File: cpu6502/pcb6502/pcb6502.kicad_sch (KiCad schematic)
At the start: 11 parts, among them J1 Power Plug, SW1 Reset, U1 6502, U2 EEPROM, U3 RAM, U4 65C22, U5 74HC00, U6 LCD (HD44780), X1 1MHz

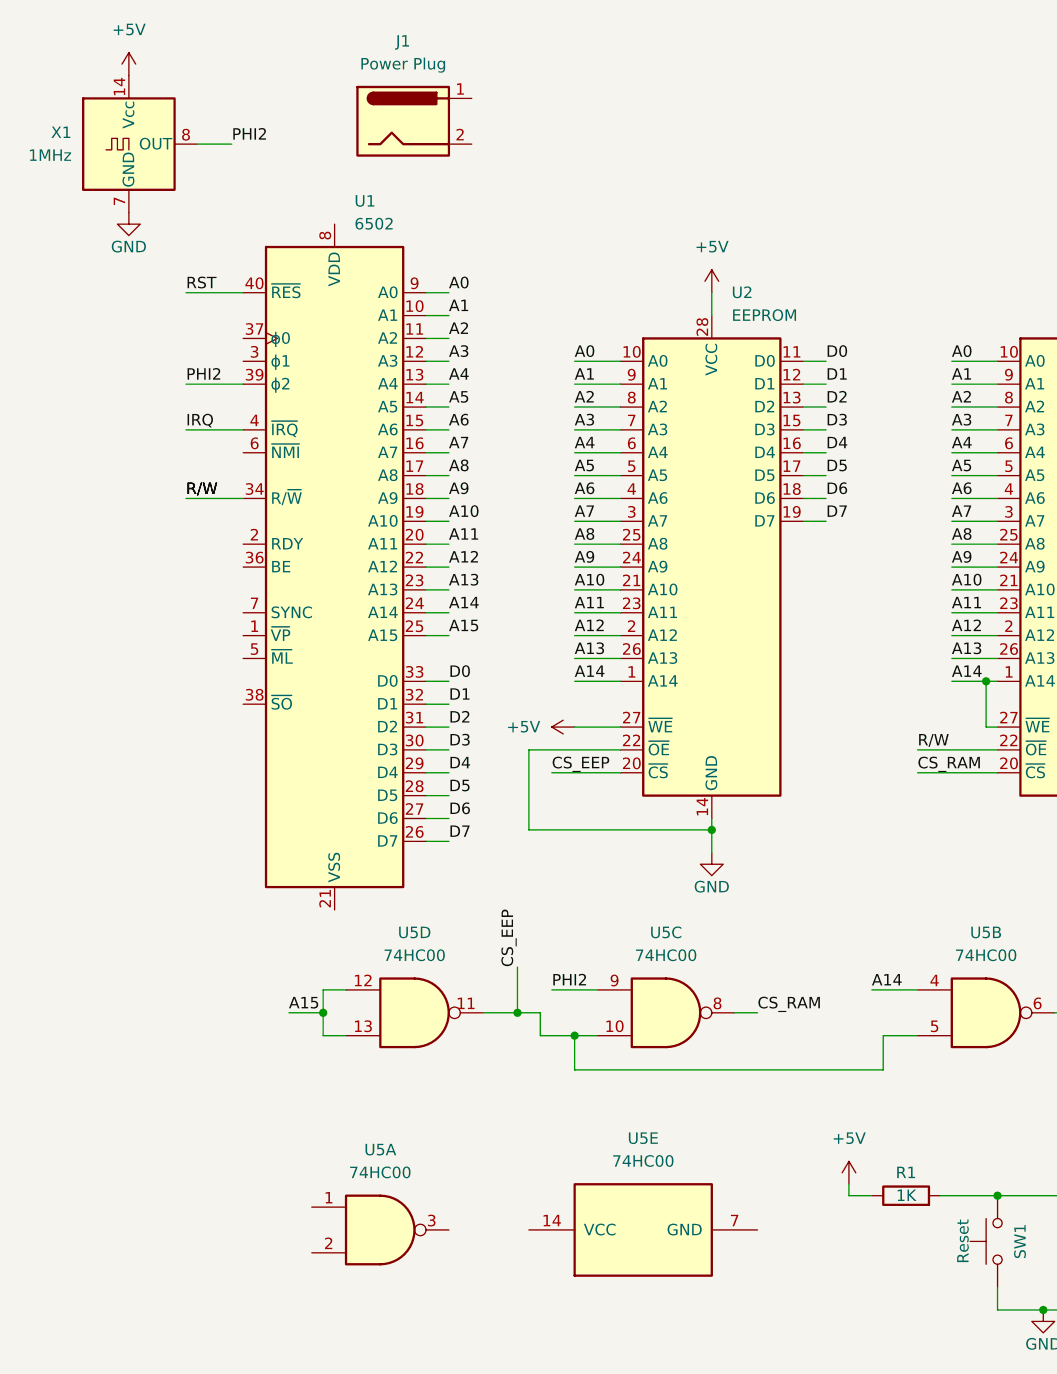
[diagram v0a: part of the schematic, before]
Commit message: connect more pins 6502 PCB
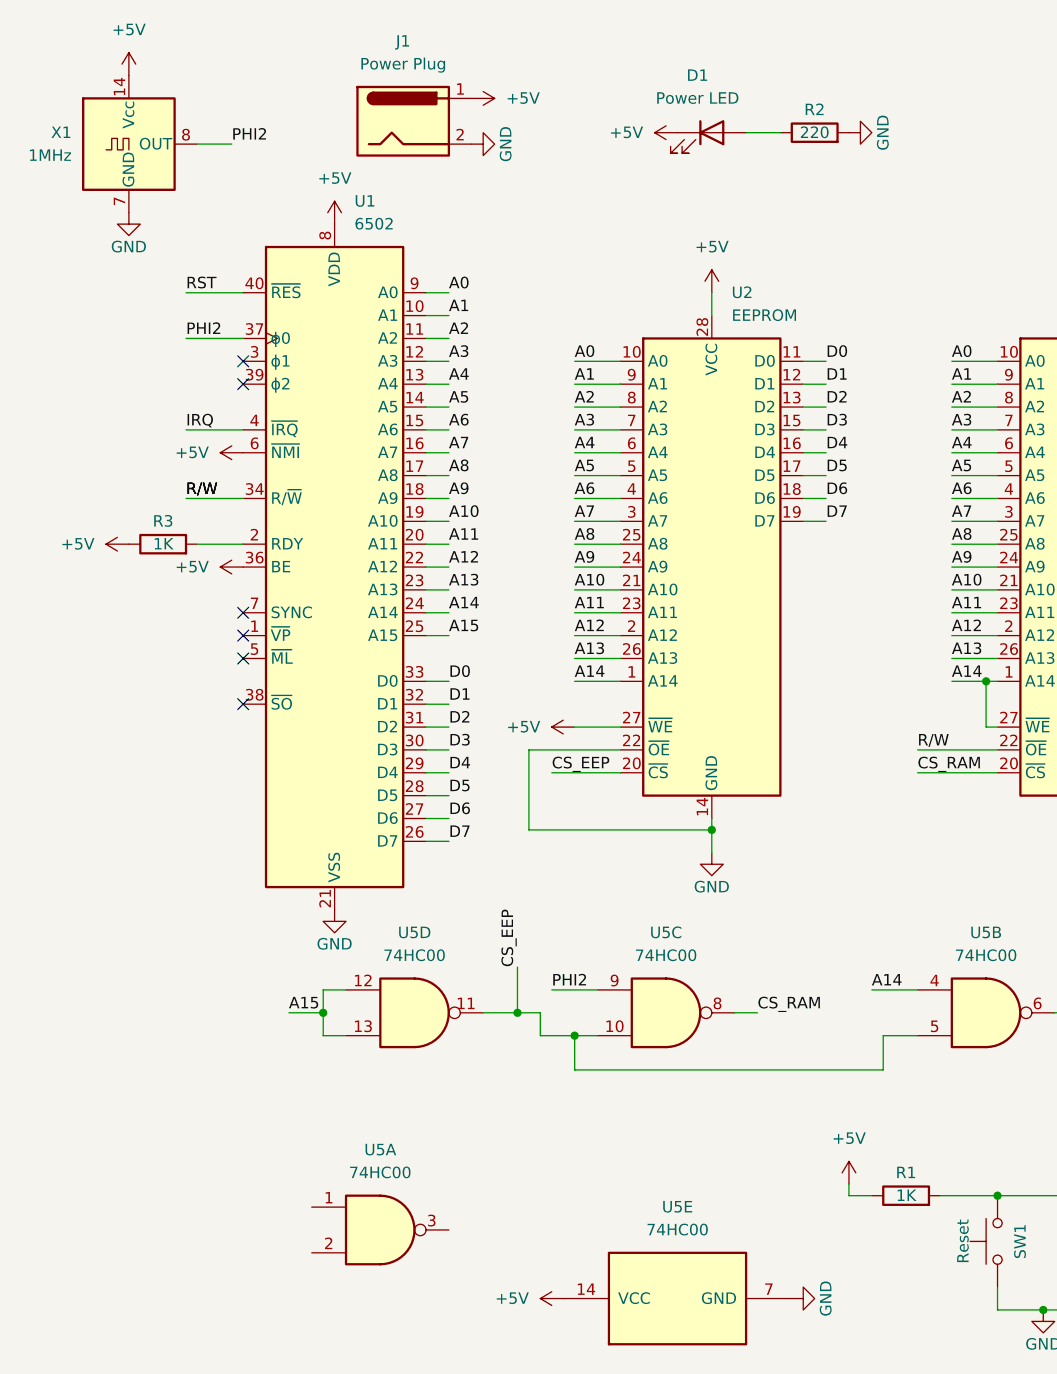
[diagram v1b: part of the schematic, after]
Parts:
- added D1: Power LED, LED_THT:LED_D5.0mm, symbol Device:LED
- added R2: 220, Resistor_THT:R_Axial_DIN0204_L3.6mm_D1.6mm_P7.62mm_Horizontal, symbol Device:R
- added R3: 1K, Resistor_THT:R_Axial_DIN0204_L3.6mm_D1.6mm_P7.62mm_Horizontal, symbol Device:R
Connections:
- net +5V: now also J1.1, U1.36 (BE), U1.6 (~{NMI}), U1.8 (VDD), U5.14 (VCC), D1.1 (K), R3.1
- net GND: now also J1.2, U1.21 (VSS), U5.7 (GND), R2.2
- net PHI2: now also U1.37 (ϕ0); no longer U1.39 (ϕ2)
- net at U1.2 (RDY): now also R3.2
- new net: D1.2 (A), R2.1
- no-connect marks 4 -> 10
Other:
- moved on the sheet: U5E

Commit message: start to add rs232
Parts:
- removed J1: Power Plug, Connector_BarrelJack:BarrelJack_Horizontal, symbol Connector:Barrel_Jack
- added C2, C3, C4, C5: 1uf, Capacitor_THT:C_Disc_D3.0mm_W1.6mm_P2.50mm, symbol Device:C
- added D2: SB140, Diode_THT:D_DO-41_SOD81_P10.16mm_Horizontal, symbol Diode:SB140
- added J1: 5v Power, Connector_BarrelJack:BarrelJack_Horizontal, symbol Connector:Barrel_Jack_MountingPin
- added J2: DE9_Receptacle, Connector_Dsub:DSUB-9_Female_Horizontal_P2.77x2.54mm_EdgePinOffset9.40mm, symbol Connector:DE9_Receptacle
- added RV1: 10K, Potentiometer_THT:Potentiometer_ACP_CA9-V10_Vertical, symbol Device:R_Potentiometer
- added U7: W65C51NxP, Package_DIP:DIP-28_W15.24mm, symbol PCM_65xx-library:W65C51NxP
- added U8: MAX232, Package_DIP:DIP-16_W7.62mm_Socket, symbol Interface_UART:MAX232
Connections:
- net +5V: now also U6.2 (LEDA), U6.4 (VDD), J1.1, U7.15 (VCC)
- net A0: now also U7.13 (RS0)
- net A1: now also U7.14 (RS1)
- net A12: now also U7.2 (CS1)
- net CS2: now also U7.3 (~{CS2})
- net D0: now also U7.18 (D0)
- net D1: now also U7.19 (D1)
- net D2: now also U7.20 (D2)
- net D3: now also U7.21 (D3)
- net D4: now also U7.22 (D4)
- net D5: now also U7.23 (D5)
- net D6: now also U7.24 (D6)
- net D7: now also U7.25 (D7)
- net GND: now also U6.3 (VSS), J1.2, J1.MP (MountPin), RV1.1, U7.1 (VSS)
- net IRQ: now also D2.2 (A)
- net PHI2: now also U7.27 (ϕ2)
- net RST: now also U7.4 (~{RES})
- net R/W: now also U7.28 (R/~{W})
- net LCD_K: now reaches U6.1 (LEDK)
- net LCD_VO: now reaches U6.5 (Vo)
- net LCD_VO: now also RV1.2
- new net: D2.1 (K), U7.26 (~{IRQ})
- no-connect marks 10 -> 11
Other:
- title: (none) -> Chris G 6502

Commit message: finish rs232, re-layour PCB
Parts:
- removed J1: 5v Power, Connector_BarrelJack:BarrelJack_Horizontal, symbol Connector:Barrel_Jack_MountingPin
- added C6: 20pf, Capacitor_THT:C_Disc_D3.0mm_W1.6mm_P2.50mm, symbol Device:C
- added J1: 5v Power, Connector_BarrelJack:BarrelJack_CUI_PJ-102AH_Horizontal, symbol Connector:Barrel_Jack_Switch_MountingPin
- added R4: 1M, Resistor_THT:R_Axial_DIN0204_L3.6mm_D1.6mm_P7.62mm_Horizontal, symbol Device:R
- added Y1: Crystal, Crystal:Crystal_HC49-4H_Vertical, symbol Device:Crystal
- J2: value DE9_Receptacle -> RS232
- U5: footprint Package_DIP:DIP-14_W7.62mm -> Package_DIP:DIP-14_W7.62mm_Socket
- U6: footprint Display:HY1602E -> Display:WC1602A
- U7: footprint Package_DIP:DIP-28_W15.24mm -> Package_DIP:DIP-28_W15.24mm_Socket
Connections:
- net +5V: now also U8.16 (VCC), J1.1
- net GND: now also C4.1, C5.2, J2.5, U8.15 (GND), C6.2, J1.2, J1.3
- net TxD: now reaches U7.10 (TxD)
- net TxD: now also U8.11 (T1IN)
- net RxD: now reaches U7.12 (RxD)
- net RxD: now also U8.12 (R1OUT)
- net XTLA1: now reaches U7.6 (XTAL1)
- net XTLA1: now also R4.2, Y1.2
- net XTAL2: now reaches U7.7 (XTAL2)
- net XTAL2: now also C6.1, R4.1, Y1.1
- net 232_VS+: now reaches C4.2
- net 232_VS+: now also U8.2 (VS+)
- net at C3.1: now also U8.4 (C2+)
- net at C3.2: now also U8.5 (C2-)
- net at U8.1 (C1+): now also C2.1
- net at U8.13 (R1IN): now also J2.3
- net at U8.14 (T1OUT): now also J2.2
- net at U8.3 (C1-): now also C2.2
- net 232_VS-: now reaches U8.6 (VS-)
- net 232_VS-: now also C5.1
- no-connect marks 11 -> 27
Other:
- moved on the sheet: C2, C3, C4, C5, J2

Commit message: routed PCB!
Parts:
- removed C1: 0.1uf, Capacitor_THT:C_Disc_D3.0mm_W1.6mm_P2.50mm, symbol Device:C
- removed J1: 5v Power, Connector_BarrelJack:BarrelJack_CUI_PJ-102AH_Horizontal, symbol Connector:Barrel_Jack_Switch_MountingPin
- removed R1: 1K, Resistor_THT:R_Axial_DIN0204_L3.6mm_D1.6mm_P7.62mm_Horizontal, symbol Device:R
- removed RV1: 10K, Potentiometer_THT:Potentiometer_ACP_CA9-V10_Vertical, symbol Device:R_Potentiometer
- removed U6: LCD (HD44780), Display:WC1602A, symbol Display_Character:HY1602E
- added C7: 1uF, Capacitor_THT:CP_Radial_D5.0mm_P2.50mm, symbol Device:C_Polarized
- added C8: 0.1uf, Capacitor_THT:C_Disc_D3.0mm_W1.6mm_P2.50mm, symbol Device:C
- added D3: 1N5819, Diode_THT:D_DO-41_SOD81_P10.16mm_Horizontal, symbol Diode:1N5819
- added H1, H2, H3, H4: ~, MountingHole:MountingHole_3.2mm_M3_Pad_Via, symbol Mechanical:MountingHole_Pad
- added J1: Power, Connector_BarrelJack:BarrelJack_Horizontal, symbol Connector:Barrel_Jack
- added J3: VIA PA, Connector_PinHeader_2.54mm:PinHeader_2x06_P2.54mm_Vertical, symbol Connector_Generic:Conn_02x06_Odd_Even
- added J4: VIA PB, Connector_PinHeader_2.54mm:PinHeader_2x06_P2.54mm_Vertical, symbol Connector_Generic:Conn_02x06_Odd_Even
- added J5: Ext RST, Connector_PinHeader_2.54mm:PinHeader_2x01_P2.54mm_Vertical, symbol Connector_Generic:Conn_02x01
- added U6: L7805, Package_TO_SOT_THT:TO-220F-3_Horizontal_TabUp, symbol Regulator_Linear:L7805
- added U9: ~, Package_TO_SOT_THT:TO-92, symbol Power_Protection:DS1813
- U2: footprint Package_DIP:DIP-28_W15.24mm_Socket -> Package_DIP:DIP-28_600_ZIF_ARIES_28-526-10
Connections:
- net +5V: now also D1.2 (A), U5.1, C8.1, J3.1 (Pin_1), J4.1 (Pin_1), U6.3 (OUT), U9.2 (VCC); no longer D1.1 (K)
- net GND: now also C7.2, C8.2, H1.1, H2.1, H3.1, H4.1, J1.2, J3.2 (Pin_2), J4.2 (Pin_2), U6.2 (GND), U9.3 (GND); no longer SW1.1
- net PA0: now also J3.5 (Pin_5)
- net PA1: now also J3.6 (Pin_6)
- net PA2: now also J3.7 (Pin_7)
- net PA3: now also J3.8 (Pin_8)
- net PA4: now also J3.9 (Pin_9)
- net PA5: now also J3.10 (Pin_10)
- net PA6: now also J3.11 (Pin_11)
- net PA7: now also J3.12 (Pin_12)
- net PB0: now also J4.5 (Pin_5)
- net PB1: now also J4.6 (Pin_6)
- net PB2: now also J4.7 (Pin_7)
- net PB3: now also J4.8 (Pin_8)
- net PB4: now also J4.9 (Pin_9)
- net PB5: now also J4.10 (Pin_10)
- net PB6: now also J4.11 (Pin_11)
- net PB7: now also J4.12 (Pin_12)
- net RST: now also J5.2 (Pin_2)
- net CB1: now reaches U4.18 (CB1)
- net CB1: now also J4.3 (Pin_3)
- net CB2: now reaches U4.19 (CB2)
- net CB2: now also J4.4 (Pin_4)
- net CA2: now reaches U4.39 (CA2)
- net CA2: now also J3.4 (Pin_4)
- net CA1: now reaches U4.40 (CA1)
- net CA1: now also J3.3 (Pin_3)
- net at R2.1: now also D1.1 (K); no longer D1.2 (A)
- new net: J5.1 (Pin_1), SW1.1, U9.1 (RST)
- new net: C7.1, D3.1 (K), U6.1 (IN)
- new net: D3.2 (A), J1.1
- no-connect marks 27 -> 22
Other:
- moved on the sheet: D1, D2, R2, SW1, U5A, U5E, U7
